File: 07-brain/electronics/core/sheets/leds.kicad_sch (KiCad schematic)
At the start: 0 parts

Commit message: Added LEDs to Brain
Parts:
- added D10, D11, D12, D13, D8, D9: LED, symbol Device:LED
- added Q10, Q11, Q6, Q7, Q8, Q9: MMBT3904, Package_TO_SOT_SMD:SOT-23, symbol Transistor_BJT:MMBT3904
- added R37, R39, R41, R43, R45, R47: 47k, Resistor_SMD:R_0603_1608Metric, symbol Device:R
- added R38, R40, R42, R44, R46, R48: 1k, Resistor_SMD:R_0603_1608Metric, symbol Device:R
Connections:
- new net: D9.1 (K), Q7.3 (C)
- new net: D9.2 (A), R40.1
- new net: D11.1 (K), Q9.3 (C)
- new net: D11.2 (A), R44.1
- new net: D13.2 (A), R48.1
- new net: Q9.1 (B), R43.2
- new net: Q11.1 (B), R47.2
- new net: D13.1 (K), Q11.3 (C)
- new net: D10.2 (A), R42.1
- new net: Q10.1 (B), R45.2
- new net: Q7.1 (B), R39.2
- new net: D8.1 (K), Q6.3 (C)
- new net: D8.2 (A), R38.1
- new net: Q6.1 (B), R37.2
- new net: D12.1 (K), Q10.3 (C)
- new net: D12.2 (A), R46.1
- new net: Q8.1 (B), R41.2
- new net: D10.1 (K), Q8.3 (C)
- new net +12V: R38.2, R40.2, R42.2, R44.2, R46.2, R48.2
- new net GND: Q10.2 (E), Q11.2 (E), Q6.2 (E), Q7.2 (E), Q8.2 (E), Q9.2 (E)
- new net GPIO_LED_1: R37.1
- new net GPIO_LED_2: R39.1
- new net GPIO_LED_3: R41.1
- new net GPIO_LED_4: R43.1
- new net GPIO_LED_5: R45.1
- new net GPIO_LED_6: R47.1

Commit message: Brain schematics WIP
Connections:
- net GPIO_LED_1 renamed LED_1
- net GPIO_LED_2 renamed LED_2
- net GPIO_LED_3 renamed LED_3
- net GPIO_LED_4 renamed LED_4
- net GPIO_LED_5 renamed LED_5
- net GPIO_LED_6 renamed LED_6
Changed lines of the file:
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@@
 		)
 	)
-	(hierarchical_label "GPIO_LED_1"
+	(hierarchical_label "LED_1"
 		(shape input)
 		(at 57.15 62.23 180)
@@
 		)
 	)
-	(hierarchical_label "GPIO_LED_3"
+	(hierarchical_label "LED_3"
 		(shape input)
 		(at 190.5 62.23 180)
@@
 		)
 	)
-	(hierarchical_label "GPIO_LED_6"
+	(hierarchical_label "LED_6"
 		(shape input)
 		(at 190.5 123.19 180)
@@
 		)
 	)
-	(hierarchical_label "GPIO_LED_5"
+	(hierarchical_label "LED_5"
 		(shape input)
 		(at 123.19 123.19 180)
@@
 		)
 	)
-	(hierarchical_label "GPIO_LED_2"
+	(hierarchical_label "LED_2"
 		(shape input)
 		(at 123.19 62.23 180)
@@
 		)
 	)
-	(hierarchical_label "GPIO_LED_4"
+	(hierarchical_label "LED_4"
 		(shape input)
 		(at 57.15 123.19 180)

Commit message: Updated Brain schematics
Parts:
- removed D10, D11, D12, D13, D9: LED, symbol Device:LED
- removed Q10, Q11, Q6, Q7, Q8, Q9: MMBT3904, Package_TO_SOT_SMD:SOT-23, symbol Transistor_BJT:MMBT3904
- removed R39, R41, R43, R45, R47: 47k, Resistor_SMD:R_0603_1608Metric, symbol Device:R
- removed R40, R42, R44, R46, R48: 1k, Resistor_SMD:R_0603_1608Metric, symbol Device:R
- added Q2: 2N3904, Package_TO_SOT_THT:TO-92_Inline, symbol Transistor_BJT:2N3904
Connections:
- net GND: now also Q2.1 (E)
- net at D8.1 (K): now also Q2.3 (C)
- net at R37.2: now also Q2.2 (B)
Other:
- moved on the sheet: D8, R37, R38

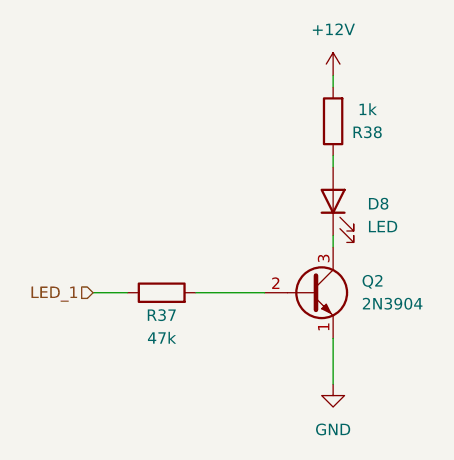
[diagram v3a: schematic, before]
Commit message: Audio/CV out BrainSDK tested/working
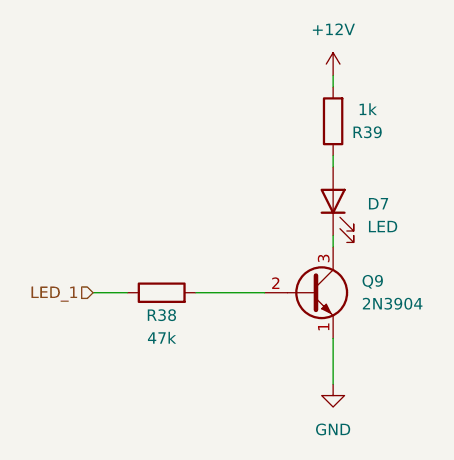
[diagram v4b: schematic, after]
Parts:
- renumbered D8 to D7, Q2 to Q9, R37 to R38, R38 to R39
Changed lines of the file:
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@@
 		(dnp no)
 		(fields_autoplaced yes)
-		(property "Reference" "#PWR054"
+		(property "Reference" "#PWR073"
 			(at 159.385 109.855 0)
 			(effects
@@
 			(project "brain-core"
 				(path "/8e2e31f3-eed5-4de1-966c-f4162758c735/58d976d6-5ff2-4f75-8bc0-3e0bd551e7f0"
-					(reference "#PWR054")
+					(reference "#PWR073")
 					(unit 1)
 				)
@@
 		(dnp no)
 		(fields_autoplaced yes)
-		(property "Reference" "Q2"
+		(property "Reference" "Q9"
 			(at 162.56 92.0749 0)
 			(effects
@@
 			(project ""
 				(path "/8e2e31f3-eed5-4de1-966c-f4162758c735/58d976d6-5ff2-4f75-8bc0-3e0bd551e7f0"
-					(reference "Q2")
+					(reference "Q9")
 					(unit 1)
 				)
@@
 		(dnp no)
 		(fields_autoplaced yes)
-		(property "Reference" "#PWR053"
+		(property "Reference" "#PWR072"
 			(at 159.385 73.025 0)
 			(effects
@@
 			(project "brain-core"
 				(path "/8e2e31f3-eed5-4de1-966c-f4162758c735/58d976d6-5ff2-4f75-8bc0-3e0bd551e7f0"
-					(reference "#PWR053")
+					(reference "#PWR072")
 					(unit 1)
 				)
@@
 		(dnp no)
 		(fields_autoplaced yes)
-		(property "Reference" "D8"
+		(property "Reference" "D7"
 			(at 163.195 83.5024 90)
 			(effects
@@
 			(project ""
 				(path "/8e2e31f3-eed5-4de1-966c-f4162758c735/58d976d6-5ff2-4f75-8bc0-3e0bd551e7f0"
-					(reference "D8")
+					(reference "D7")
 					(unit 1)
 				)
@@
 		(on_board yes)
 		(dnp no)
-		(property "Reference" "R38"
+		(property "Reference" "R39"
 			(at 163.195 75.565 0)
 			(effects
@@
 			(project "brain-core"
 				(path "/8e2e31f3-eed5-4de1-966c-f4162758c735/58d976d6-5ff2-4f75-8bc0-3e0bd551e7f0"
-					(reference "R38")
+					(reference "R39")
 					(unit 1)
 				)
@@
 		(on_board yes)
 		(dnp no)
-		(property "Reference" "R37"
+		(property "Reference" "R38"
 			(at 140.335 95.885 90)
 			(effects
@@
 			(project "brain-core"
 				(path "/8e2e31f3-eed5-4de1-966c-f4162758c735/58d976d6-5ff2-4f75-8bc0-3e0bd551e7f0"
-					(reference "R37")
+					(reference "R38")
 					(unit 1)
 				)

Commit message: Design Brain/Core PCB
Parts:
- renumbered D7 to #D7, Q9 to #Q9, R38 to #R38, R39 to #R39
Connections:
- net LED_1: no longer names the net of #R38.1
- no-connect marks 0 -> 1
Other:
- note added: "LED_1-6"
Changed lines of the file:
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@@
 	(generator_version "9.0")
 	(paper "A4")
+	(text "LED_1-6"
+		(exclude_from_sim no)
+		(at 139.7 93.98 0)
+		(effects
+			(font
+				(size 1.27 1.27)
+			)
+		)
+	)
+	(no_connect
+		(at 144.78 93.98)
+	)
 	(wire
 		(pts
-			(xy 159.385 86.995) (xy 159.385 88.265)
+			(xy 160.02 104.14) (xy 160.02 99.06)
 		)
 		(stroke
@@
 		)
 	)
-	(wire
-		(pts
-			(xy 159.385 69.215) (xy 159.385 70.485)
-		)
-		(stroke
-			(width 0)
-			(type default)
-		)
-	)
-	(wire
-		(pts
-			(xy 159.385 103.505) (xy 159.385 98.425)
-		)
-		(stroke
-			(width 0)
-			(type default)
-		)
-	)
-	(wire
-		(pts
-			(xy 132.715 93.345) (xy 136.525 93.345)
-		)
-		(stroke
-			(width 0)
-			(type default)
-		)
-	)
-	(wire
-		(pts
-			(xy 144.145 93.345) (xy 151.765 93.345)
-		)
-		(stroke
-			(width 0)
-			(type default)
-		)
-	)
-	(wire
-		(pts
-			(xy 159.385 78.105) (xy 159.385 79.375)
-		)
-		(stroke
-			(width 0)
-			(type default)
-		)
-	)
-	(hierarchical_label "LED_1"
-		(shape input)
-		(at 132.715 93.345 180)
-		(effects
-			(font
-				(size 1.27 1.27)
-			)
-			(justify right)
-		)
-	)
 	(symbol
 		(lib_id "power:GND")
-		(at 159.385 103.505 0)
+		(at 160.02 104.14 0)
 		(unit 1)
 		(exclude_from_sim no)
@@
 		(fields_autoplaced yes)
 		(property "Reference" "#PWR073"
-			(at 159.385 109.855 0)
+			(at 160.02 110.49 0)
 			(effects
 				(font
@@
 		)
 		(property "Value" "GND"
-			(at 159.385 108.585 0)
+			(at 160.02 109.22 0)
 			(effects
 				(font
@@
 		)
 		(property "Footprint" ""
-			(at 159.385 103.505 0)
+			(at 160.02 104.14 0)
 			(effects
 				(font
@@
 		)
 		(property "Datasheet" ""
-			(at 159.385 103.505 0)
+			(at 160.02 104.14 0)
 			(effects
 				(font
@@
 		)
 		(property "Description" "Power symbol creates a global label with name \"GND\" , ground"
-			(at 159.385 103.505 0)
+			(at 160.02 104.14 0)
 			(effects
 				(font
@@
 	(symbol
 		(lib_id "Transistor_BJT:2N3904")
-		(at 156.845 93.345 0)
+		(at 157.48 93.98 0)
 		(unit 1)
 		(exclude_from_sim no)
@@
 		(dnp no)
 		(fields_autoplaced yes)
-		(property "Reference" "Q9"
-			(at 162.56 92.0749 0)
+		(property "Reference" "#Q9"
+			(at 163.195 92.7099 0)
 			(effects
 				(font
@@
 		)
 		(property "Value" "2N3904"
-			(at 162.56 94.6149 0)
+			(at 163.195 95.2499 0)
 			(effects
 				(font
@@
 		)
 		(property "Footprint" "Package_TO_SOT_THT:TO-92_Inline"
-			(at 161.925 95.25 0)
+			(at 162.56 95.885 0)
 			(effects
 				(font
@@
 		)
 		(property "Datasheet" "https://www.onsemi.com/pub/Collateral/2N3903-D.PDF"
-			(at 156.845 93.345 0)
+			(at 157.48 93.98 0)
 			(effects
 				(font
@@
 		)
 		(property "Description" "0.2A Ic, 40V Vce, Small Signal NPN Transistor, TO-92"
-			(at 156.845 93.345 0)
+			(at 157.48 93.98 0)
 			(effects
 				(font
@@
 			(project ""
 				(path "/8e2e31f3-eed5-4de1-966c-f4162758c735/58d976d6-5ff2-4f75-8bc0-3e0bd551e7f0"
-					(reference "Q9")
+					(reference "#Q9")
 					(unit 1)
 				)
@@
 	(symbol
 		(lib_id "power:+12V")
-		(at 159.385 69.215 0)
+		(at 160.02 73.66 0)
 		(unit 1)
 		(exclude_from_sim no)
@@
 		(fields_autoplaced yes)
 		(property "Reference" "#PWR072"
-			(at 159.385 73.025 0)
+			(at 160.02 77.47 0)
 			(effects
 				(font
@@
 		)
 		(property "Value" "+12V"
-			(at 159.385 64.135 0)
+			(at 160.02 68.58 0)
 			(effects
 				(font
@@
 		)
 		(property "Footprint" ""
-			(at 159.385 69.215 0)
+			(at 160.02 73.66 0)
 			(effects
 				(font
@@
 		)
 		(property "Datasheet" ""
-			(at 159.385 69.215 0)
+			(at 160.02 73.66 0)
 			(effects
 				(font
@@
 		)
 		(property "Description" "Power symbol creates a global label with name \"+12V\""
-			(at 159.385 69.215 0)
+			(at 160.02 73.66 0)
 			(effects
 				(font
@@
 	(symbol
 		(lib_id "Device:LED")
-		(at 159.385 83.185 90)
+		(at 160.02 85.09 90)
 		(unit 1)
 		(exclude_from_sim no)
@@
 		(dnp no)
 		(fields_autoplaced yes)
-		(property "Reference" "D7"
-			(at 163.195 83.5024 90)
-			(effects
-				(font
-					(size 1.27 1.27)
-				)
-				(justify right)
+		(property "Reference" "#D7"
+			(at 156.845 85.4074 90)
+			(effects
+				(font
+					(size 1.27 1.27)
+				)
+				(justify left)
 			)
 		)
 		(property "Value" "LED"
-			(at 163.195 86.0424 90)
-			(effects
-				(font
-					(size 1.27 1.27)
-				)
-				(justify right)
+			(at 156.845 87.9474 90)
+			(effects
+				(font
+					(size 1.27 1.27)
+				)
+				(justify left)
 			)
 		)
 		(property "Footprint" ""
-			(at 159.385 83.185 0)
+			(at 160.02 85.09 0)
 			(effects
 				(font
@@
 		)
 		(property "Datasheet" "~"
-			(at 159.385 83.185 0)
+			(at 160.02 85.09 0)
 			(effects
 				(font
@@
 		)
 		(property "Description" "Light emitting diode"
-			(at 159.385 83.185 0)
+			(at 160.02 85.09 0)
 			(effects
 				(font
@@
 		)
 		(property "Sim.Pins" "1=K 2=A"
-			(at 159.385 83.185 0)
+			(at 160.02 85.09 0)
 			(effects
 				(font
@@
 			(project ""
 				(path "/8e2e31f3-eed5-4de1-966c-f4162758c735/58d976d6-5ff2-4f75-8bc0-3e0bd551e7f0"
-					(reference "D7")
+					(reference "#D7")
 					(unit 1)
 				)
@@
 	(symbol
 		(lib_id "Device:R")
-		(at 159.385 74.295 180)
+		(at 160.02 77.47 180)
 		(unit 1)
 		(exclude_from_sim no)
@@
 		(on_board yes)
 		(dnp no)
-		(property "Reference" "R39"
-			(at 163.195 75.565 0)
+		(property "Reference" "#R39"
+			(at 163.83 78.74 0)
 			(effects
 				(font
@@
 		)
 		(property "Value" "1k"
-			(at 163.195 73.025 0)
+			(at 163.83 76.2 0)
 			(effects
 				(font
@@
 		)
 		(property "Footprint" "Resistor_SMD:R_0603_1608Metric"
-			(at 161.163 74.295 90)
+			(at 161.798 77.47 90)
 			(effects
 				(font
@@
 		)
 		(property "Datasheet" "~"
-			(at 159.385 74.295 0)
+			(at 160.02 77.47 0)
 			(effects
 				(font
@@
 		)
 		(property "Description" ""
-			(at 159.385 74.295 0)
+			(at 160.02 77.47 0)
 			(effects
 				(font
@@
 		)
 		(property "LCSC" ""
-			(at 159.385 74.295 90)
+			(at 160.02 77.47 90)
 			(effects
 				(font
@@
 		)
 		(property "Mouser" ""
-			(at 159.385 74.295 0)
+			(at 160.02 77.47 0)
 			(effects
 				(font
@@
 		)
 		(property "Part No." ""
-			(at 159.385 74.295 0)
+			(at 160.02 77.47 0)
 			(effects
 				(font
@@
 		)
 		(property "Part URL" ""
-			(at 159.385 74.295 0)
+			(at 160.02 77.47 0)
 			(effects
 				(font
@@
 		)
 		(property "Vendor" "JLCPCB"
-			(at 159.385 74.295 0)
+			(at 160.02 77.47 0)
 			(effects
 				(font
@@
 		)
 		(property "Field4" ""
-			(at 159.385 74.295 0)
+			(at 160.02 77.47 0)
 			(effects
 				(font
@@
 			(project "brain-core"
 				(path "/8e2e31f3-eed5-4de1-966c-f4162758c735/58d976d6-5ff2-4f75-8bc0-3e0bd551e7f0"
-					(reference "R39")
+					(reference "#R39")
 					(unit 1)
 				)
@@
 	(symbol
 		(lib_id "Device:R")
-		(at 140.335 93.345 90)
+		(at 148.59 93.98 90)
 		(unit 1)
 		(exclude_from_sim no)
@@
 		(on_board yes)
 		(dnp no)
-		(property "Reference" "R38"
-			(at 140.335 95.885 90)
+		(property "Reference" "#R38"
+			(at 148.59 96.52 90)
 			(effects
 				(font
@@
 		)
 		(property "Value" "47k"
-			(at 140.335 98.425 90)
+			(at 148.59 99.06 90)
 			(effects
 				(font
@@
 		)
 		(property "Footprint" "Resistor_SMD:R_0603_1608Metric"
-			(at 140.335 95.123 90)
+			(at 148.59 95.758 90)
 			(effects
 				(font
@@
 		)
 		(property "Datasheet" "~"
-			(at 140.335 93.345 0)
+			(at 148.59 93.98 0)
 			(effects
 				(font
@@
 		)
 		(property "Description" ""
-			(at 140.335 93.345 0)
+			(at 148.59 93.98 0)
 			(effects
 				(font
@@
 		)
 		(property "LCSC" "C25803"
-			(at 140.335 93.345 90)
+			(at 148.59 93.98 90)
 			(effects
 				(font
@@
 		)
 		(property "Mouser" ""
-			(at 140.335 93.345 0)
+			(at 148.59 93.98 0)
 			(effects
 				(font
@@
 		)
 		(property "Part No." ""
-			(at 140.335 93.345 0)
+			(at 148.59 93.98 0)
 			(effects
 				(font
@@
 		)
 		(property "Part URL" ""
-			(at 140.335 93.345 0)
+			(at 148.59 93.98 0)
 			(effects
 				(font
@@
 		)
 		(property "Vendor" "JLCPCB"
-			(at 140.335 93.345 0)
+			(at 148.59 93.98 0)
 			(effects
 				(font
@@
 		)
 		(property "Field4" ""
-			(at 140.335 93.345 0)
+			(at 148.59 93.98 0)
 			(effects
 				(font
@@
 			(project "brain-core"
 				(path "/8e2e31f3-eed5-4de1-966c-f4162758c735/58d976d6-5ff2-4f75-8bc0-3e0bd551e7f0"
-					(reference "R38")
+					(reference "#R38")
 					(unit 1)
 				)
